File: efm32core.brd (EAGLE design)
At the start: 52.1 x 53.3 mm, 7 parts

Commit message: marching on
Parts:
- added C1, C2: (no value), maple-r5:UD-4X5,8_NICHICON
- added C3: 0.1uF, SparkFun-Capacitors:0603-CAP
- added PMIC1: MCP1700T-DIGITAL, maple-r5:SOT23
- added PMIC2: MCP1700T-ANALOG, maple-r5:SOT23
- added R1: 100, SparkFun-Resistors:0603-RES
- added S1: SWITCH-MOMENTARY-2SMD, SparkFun-Electromechanical:TACTILE_SWITCH_SMD
- added USB: PIXHAWK2_MOLEX-47346-0001, PX4FMUv1.7.1:PIXHAWK2_MOLEX-47346-0001
- moved U$7 12.0 mm to (33.5, 19.1), turned to 270 degrees
- moved U$5 8.90 mm to (5.54, 25.8)
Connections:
- new net 3.3V: C1.+, PMIC1.2
- new net GND: C1.-, C2.-, C3.1, PMIC1.1, PMIC2.1, R1.1, USB.GND, USB.GND1, USB.GND2, USB.GND3
- new net N$5: C3.2, S1.3, U$7.20
- new net N$6: R1.2, S1.1
- new net VDD: C2.+, PMIC2.2
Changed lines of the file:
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@@
 <layer number="54" name="bGND_GNDA" color="1" fill="9" visible="no" active="no"/>
 <layer number="56" name="wert" color="7" fill="1" visible="no" active="no"/>
+<layer number="57" name="tCAD" color="7" fill="1" visible="yes" active="yes"/>
+<layer number="58" name="bCAD" color="7" fill="1" visible="yes" active="yes"/>
 <layer number="91" name="Nets" color="2" fill="1" visible="no" active="no"/>
 <layer number="92" name="Busses" color="1" fill="1" visible="no" active="no"/>
@@
 <layer number="108" name="tplace-old" color="10" fill="1" visible="yes" active="yes"/>
 <layer number="109" name="ref-old" color="11" fill="1" visible="yes" active="yes"/>
+<layer number="110" name="fp0" color="7" fill="1" visible="yes" active="yes"/>
 <layer number="116" name="Patch_BOT" color="9" fill="4" visible="no" active="yes"/>
 <layer number="121" name="_tsilk" color="7" fill="1" visible="no" active="yes"/>
 <layer number="122" name="_bsilk" color="7" fill="1" visible="no" active="yes"/>
+<layer number="123" name="tTestmark" color="7" fill="1" visible="yes" active="yes"/>
+<layer number="124" name="bTestmark" color="7" fill="1" visible="yes" active="yes"/>
 <layer number="125" name="_tNames" color="7" fill="1" visible="yes" active="yes"/>
+<layer number="131" name="tAdjust" color="7" fill="1" visible="yes" active="yes"/>
+<layer number="132" name="bAdjust" color="7" fill="1" visible="yes" active="yes"/>
 <layer number="144" name="Drill_legend" color="7" fill="1" visible="yes" active="yes"/>
 <layer number="151" name="HeatSink" color="7" fill="1" visible="no" active="yes"/>
@@
 <wire x1="29.21" y1="50.8" x2="25.146" y2="50.8" width="0.254" layer="37"/>
 <wire x1="34.29" y1="2.54" x2="30.226" y2="2.54" width="0.254" layer="37"/>
-<wire x1="7.366" y1="50.8" x2="2.54" y2="50.8" width="0.254" layer="37"/>
 <dimension x1="49.53" y1="40.64" x2="49.53" y2="53.34" x3="61.468" y3="46.99" textsize="1.27" layer="37"/>
 <dimension x1="49.53" y1="2.54" x2="49.53" y2="0" x3="60.96" y3="1.27" textsize="1.27" layer="37"/>
@@
 </autorouter>
 <elements>
-<element name="U$5" library="gecko" package="GECKO_SOLDER_MASK_BOTTOM" value="" x="5.028" y="34.686" rot="MR0"/>
-<element name="U$7" library="EnergyMicro" package="QFP64" value="EFM32LG332F256" x="25.146" y="27.686"/>
+<element name="U$5" library="gecko" package="GECKO_SOLDER_MASK_BOTTOM" value="" x="5.536" y="25.796" rot="MR0"/>
+<element name="U$7" library="EnergyMicro" package="QFP64" value="EFM32LG332F256" x="33.528" y="19.05" rot="R270"/>
 <element name="JIOH" library="SparkFun-Connectors" package="1X08" value="" x="25.146" y="50.8" rot="R180"/>
 <element name="JIOL" library="SparkFun-Connectors" package="1X08" value="" x="46.99" y="50.8" rot="R180"/>
@@
 <element name="JPOWER" library="SparkFun-Connectors" package="1X06" value="" x="17.526" y="2.54"/>
 <element name="JEX" library="SparkFun-Connectors" package="2X8" value="M08X2" x="49.53" y="12.7" rot="R90"/>
+<element name="PMIC1" library="maple-r5" package="SOT23" value="MCP1700T-DIGITAL" x="10.922" y="9.398"/>
+<element name="PMIC2" library="maple-r5" package="SOT23" value="MCP1700T-ANALOG" x="15.24" y="9.398"/>
+<element name="C1" library="maple-r5" package="UD-4X5,8_NICHICON" value="" x="13.208" y="33.528" rot="R270"/>
+<element name="C2" library="maple-r5" package="UD-4X5,8_NICHICON" value="" x="13.208" y="41.148" rot="R90"/>
+<element name="S1" library="SparkFun-Electromechanical" package="TACTILE_SWITCH_SMD" value="SWITCH-MOMENTARY-2SMD" x="3.048" y="48.768" rot="R90"/>
+<element name="R1" library="SparkFun-Resistors" package="0603-RES" value="100" x="2.032" y="43.434" rot="R90">
+<attribute name="PROD_ID" value="RES-07863" x="2.032" y="43.434" size="1.778" layer="27" rot="R90" display="off"/>
+</element>
+<element name="C3" library="SparkFun-Capacitors" package="0603-CAP" value="0.1uF" x="4.572" y="43.434" rot="R90">
+<attribute name="PROD_ID" value="CAP-08604" x="4.572" y="43.434" size="1.778" layer="27" rot="R90" display="off"/>
+</element>
+<element name="USB" library="PX4FMUv1.7.1" package="PIXHAWK2_MOLEX-47346-0001" value="PIXHAWK2_MOLEX-47346-0001" x="2.286" y="7.112"/>
 </elements>
 <signals>
@@
 <contactref element="U$7" pad="22"/>
 <contactref element="U$7" pad="56"/>
-<wire x1="23.896" y1="21.936" x2="19.396" y2="27.936" width="0" layer="19" extent="16-16"/>
-<wire x1="25.396" y1="33.436" x2="19.396" y2="27.936" width="0" layer="19" extent="16-16"/>
+<wire x1="33.778" y1="24.8" x2="39.278" y2="18.8" width="0" layer="19" extent="1-1"/>
+<wire x1="27.778" y1="20.3" x2="33.778" y2="24.8" width="0" layer="19" extent="1-1"/>
 </signal>
 <signal name="N$1">
@@
 <contactref element="JPOWER" pad="1"/>
 </signal>
+<signal name="3.3V">
+<contactref element="PMIC1" pad="2"/>
+<contactref element="C1" pad="+"/>
+<wire x1="11.872" y1="8.298" x2="13.208" y2="31.849" width="0" layer="19" extent="1-1"/>
+</signal>
+<signal name="VDD">
+<contactref element="PMIC2" pad="2"/>
+<contactref element="C2" pad="+"/>
+<wire x1="16.19" y1="8.298" x2="13.208" y2="42.827" width="0" layer="19" extent="1-1"/>
+</signal>
+<signal name="GND">
+<contactref element="C1" pad="-"/>
+<contactref element="PMIC1" pad="1"/>
+<contactref element="PMIC2" pad="1"/>
+<contactref element="C2" pad="-"/>
+<contactref element="R1" pad="1"/>
+<contactref element="C3" pad="1"/>
+<contactref element="USB" pad="GND"/>
+<contactref element="USB" pad="GND1"/>
+<contactref element="USB" pad="GND2"/>
+<contactref element="USB" pad="GND3"/>
+<wire x1="13.208" y1="35.207" x2="13.208" y2="39.469" width="0" layer="19" extent="1-1"/>
+<wire x1="4.572" y1="42.584" x2="13.208" y2="39.469" width="0" layer="19" extent="1-1"/>
+<wire x1="2.032" y1="42.584" x2="4.572" y2="42.584" width="0" layer="19" extent="1-1"/>
+<wire x1="14.29" y1="8.298" x2="13.208" y2="35.207" width="0" layer="19" extent="1-1"/>
+<wire x1="9.972" y1="8.298" x2="14.29" y2="8.298" width="0" layer="19" extent="1-1"/>
+<wire x1="5.086" y1="5.812" x2="9.972" y2="8.298" width="0" layer="19" extent="1-1"/>
+<wire x1="4.586" y1="4.612" x2="5.086" y2="5.812" width="0" layer="19" extent="1-1"/>
+<wire x1="4.586" y1="9.612" x2="5.086" y2="5.812" width="0" layer="19" extent="1-1"/>
+<wire x1="2.286" y1="10.062" x2="4.586" y2="9.612" width="0" layer="19" extent="1-1"/>
+</signal>
+<signal name="N$5">
+<contactref element="U$7" pad="20"/>
+<contactref element="S1" pad="3"/>
+<contactref element="C3" pad="2"/>
+<wire x1="4.572" y1="44.284" x2="4.953" y2="46.228" width="0" layer="19" extent="1-1"/>
+<wire x1="27.778" y1="21.3" x2="4.572" y2="44.284" width="0" layer="19" extent="1-1"/>
+</signal>
+<signal name="N$6">
+<contactref element="S1" pad="1"/>
+<contactref element="R1" pad="2"/>
+<wire x1="2.032" y1="44.284" x2="1.143" y2="46.228" width="0" layer="19" extent="1-1"/>
+</signal>
 </signals>

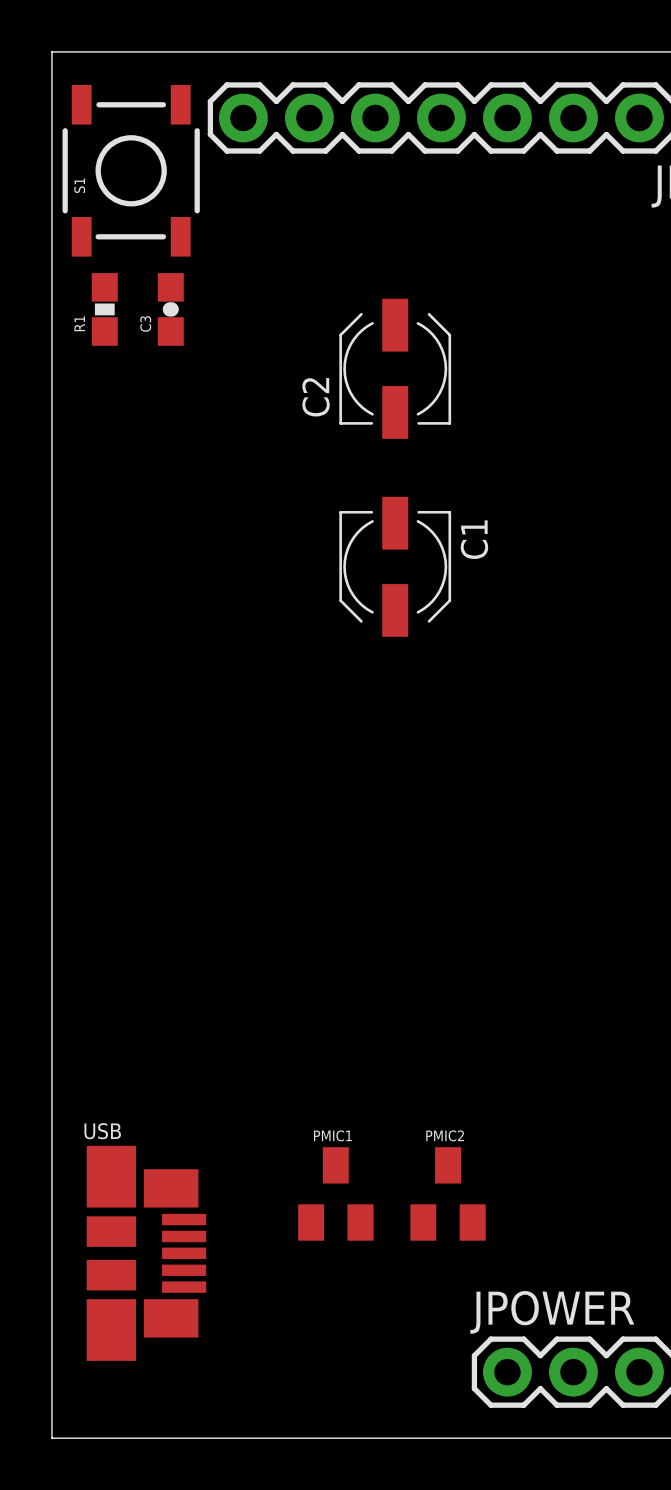
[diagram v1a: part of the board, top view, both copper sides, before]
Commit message: optimize board shape
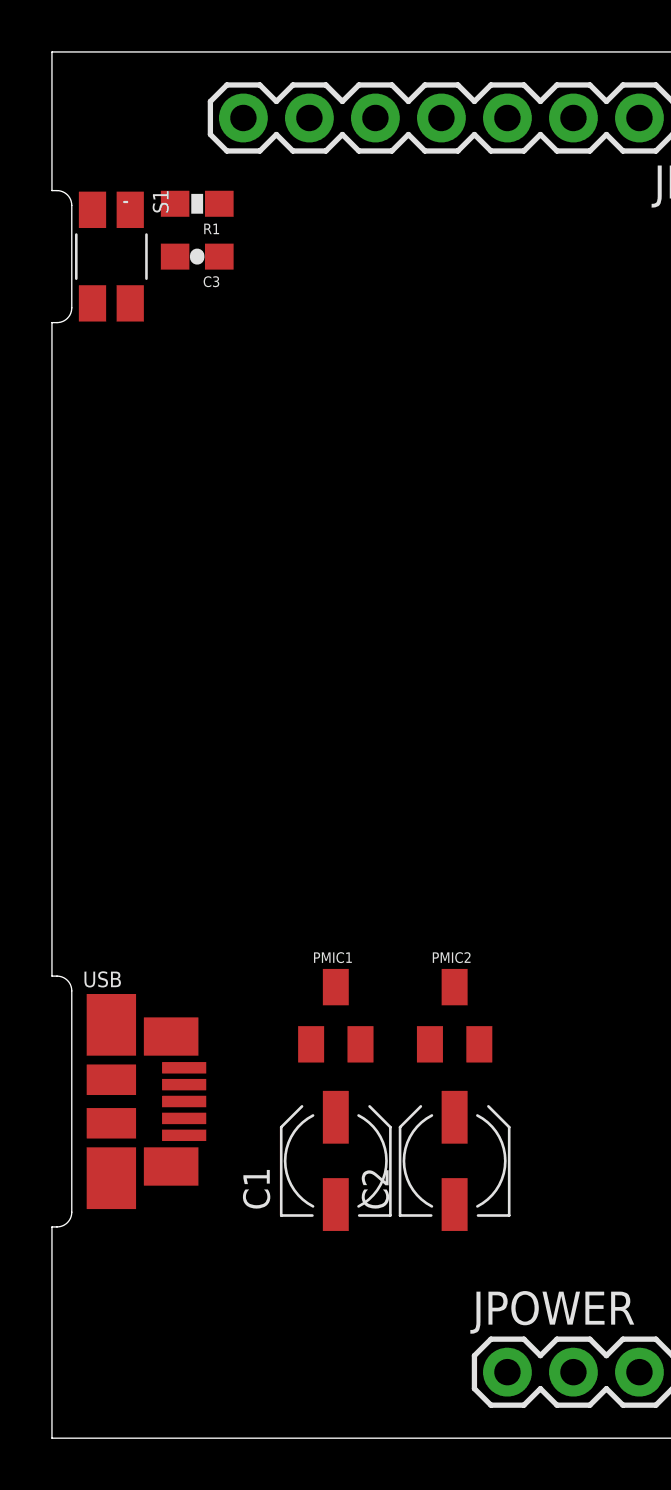
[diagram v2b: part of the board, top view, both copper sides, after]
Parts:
- S1: value SWITCH-MOMENTARY-2SMD -> PIXHAWK2_SWITCH-MOMENTARY-2; device SparkFun-Electromechanical:TACTILE_SWITCH_SMD -> PX4FMUv1.7.1:PIXHAWK2_EVQP7J01K
- moved C2 30.6 mm to (15.5, 10.7)
- moved U$5 29.6 mm to (34.4, 19.3), turned to 270 degrees
- moved C1 23.0 mm to (10.9, 10.7), turned to 90 degrees
- moved PMIC2 6.86 mm to (15.5, 16.3)
- moved PMIC1 6.86 mm to (10.9, 16.3)
- moved USB 5.84 mm to (2.29, 13.0)
- moved R1 5.40 mm to (5.59, 47.5), turned to 180 degrees
- moved S1 3.39 mm to (2.29, 45.5), turned to 270 degrees
- moved C3 2.27 mm to (5.59, 45.5), turned to 180 degrees
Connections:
- new net 5V: PMIC1.3, PMIC2.3, USB.VBUS
- net N$5: now also S1.B3; no longer S1.3
- net N$6: now also S1.A1; no longer S1.1
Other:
- outline, holes or cut-outs redrawn

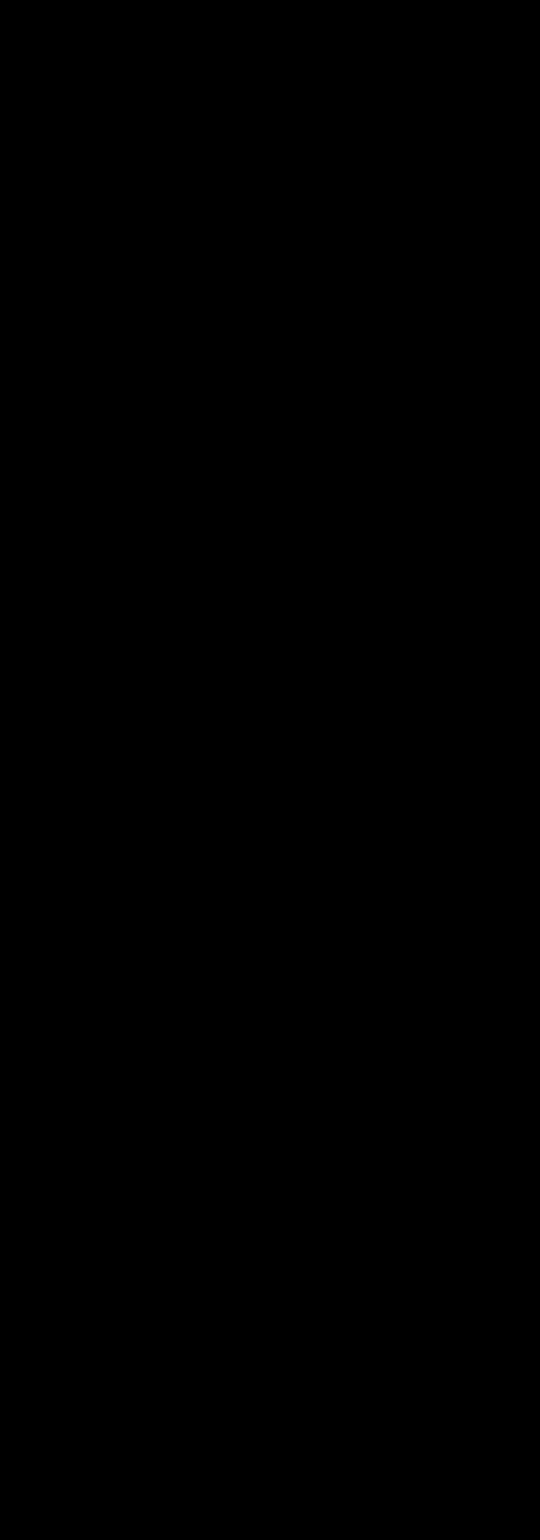
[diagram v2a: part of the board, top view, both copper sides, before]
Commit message: modulize, update power and usb
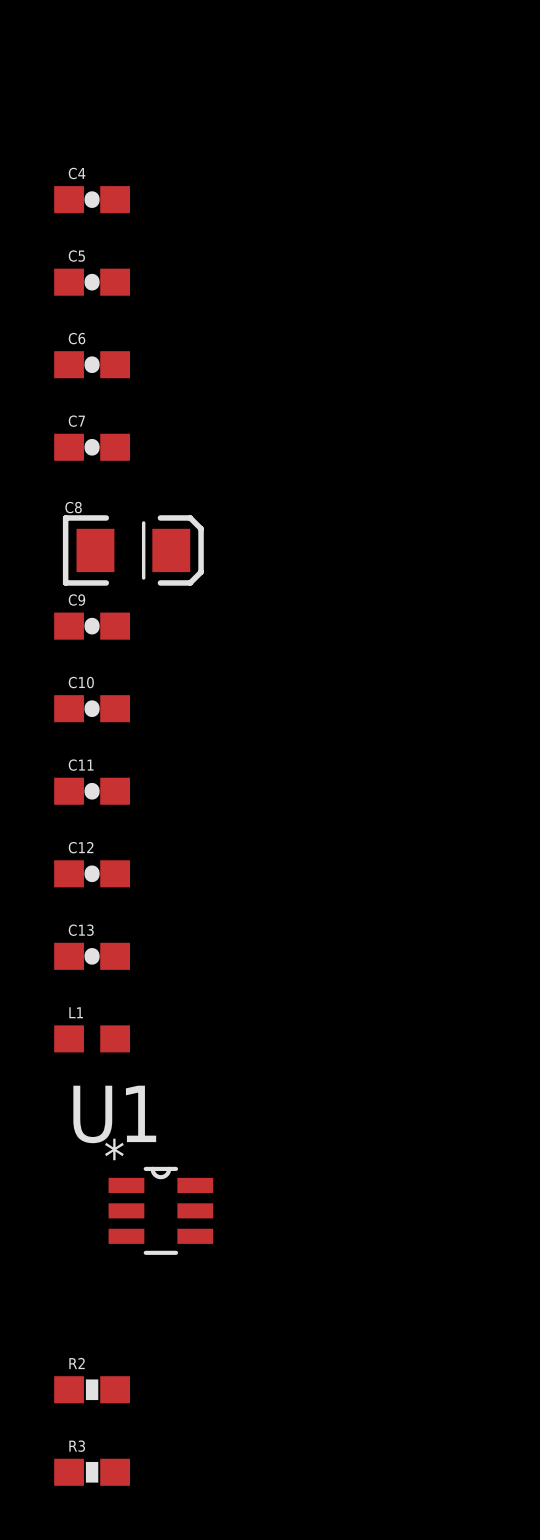
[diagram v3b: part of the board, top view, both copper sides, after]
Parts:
- added C10: 4.7uF, SparkFun-Capacitors:0603-CAP
- added C11, C12: 10nF, SparkFun-Capacitors:0603-CAP
- added C13: 10uF, SparkFun-Capacitors:0603-CAP
- added C4, C9: 1.0uF, SparkFun-Capacitors:0603-CAP
- added C5, C6, C7: 0.1uF, SparkFun-Capacitors:0603-CAP
- added C8: 10uF, SparkFun-Capacitors:EIA3216
- added L1: (no value), SparkFun-Passives:0603
- added R2, R3: 15R, SparkFun-Resistors:0603-RES
- added U1: IP4220CZ6SSOT-6, FT232H-basic:SOT95P275X110-6N
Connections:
- removed net AVDD_0: U$7.27
- removed net AVDD_1: U$7.23
- removed net DECOUPLE: U$7.40
- removed net IOVDD_0: U$7.7
- removed net IOVDD_3: U$7.26
- removed net IOVDD_5: U$7.55
- removed net USB_VBUS: U$7.52
- removed net USB_VREGI: U$7.45
- removed net USB_VREGO: U$7.46
- removed net VDD_DREG: U$7.39
- removed net VSS: U$7.22, U$7.56, U$7.8
- new net 1: L1.2, U1.5, USB.VBUS
- new net N$10: C11.1, C12.1, C13.1, U$7.23, U$7.27
- new net N$13: R3.2, U1.4, USB.D+
- new net N$14: R2.2, U1.6, USB.D-
- new net N$7: C4.1, U$7.40
- new net N$8: C9.2, U$7.46
- new net USB_DM: R2.1, U$7.47
- new net USB_DP: R3.1, U$7.48
- new net USB_ID: U$7.53, U1.1, USB.ID
- net 5V: now also C10.2, C5.2, C6.2, C7.2, C8.A, L1.1, U$7.26, U$7.39, U$7.45, U$7.52, U$7.55, U$7.7; no longer USB.VBUS
- net GND: now also C10.1, C11.2, C12.2, C13.2, C4.2, C5.1, C6.1, C7.1, C8.C, C9.1, U$7.22, U$7.56, U$7.8, U1.2, USB.GND4

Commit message: optimize a bit
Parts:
- added C14: 1uF, SparkFun-Capacitors:1206
- added STANDOFF1, STANDOFF2, STANDOFF3, STANDOFF4: STAND-OFF, SparkFun-Electromechanical:STAND-OFF
- C1, C2: value (none) -> 1uF; device maple-r5:UD-4X5,8_NICHICON -> SparkFun-Capacitors:1206
- C13: device SparkFun-Capacitors:0603-CAP -> SparkFun-Capacitors:1206
- C8: device SparkFun-Capacitors:EIA3216 -> SparkFun-Capacitors:1206
- moved C2 87.8 mm to (-13.7, -72.1), turned to 0 degrees
- moved C1 82.7 mm to (-13.7, -68.3), turned to 0 degrees
- moved C8 38.4 mm to (-13.7, -60.7)
- moved C13 27.1 mm to (-13.7, -64.5)
- moved USB 1.78 mm to (2.29, 11.2)
- moved C3 0.25 mm to (5.59, 45.2)
- moved R1 0.25 mm to (5.59, 47.2)
- moved S1 0.25 mm to (2.29, 45.2)
- renumbered U$5 to GECKO, U$7 to MCU
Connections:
- removed net N$4: JPOWER.1
- removed net N$5: C3.2, MCU.20, S1.B3
- new net ADCH0: MCU.28
- new net ADCH1: MCU.29
- new net ADCH2: MCU.30
- new net ADCH3: MCU.31
- new net ADCH4: MCU.32
- new net ADCH5: MCU.33
- new net PD6: MCU.34
- new net PD7: MCU.35
- new net PD8: MCU.36
- new net RESET: C3.2, JPOWER.1, MCU.20, S1.B3
- new net VIN: JPOWER.6
- net 3.3V: now also C1.1, JPOWER.2; no longer C1.+
- net 5V: now also C14.1, C8.2; no longer C8.A
- net GND: now also C1.2, C14.2, C2.2, C8.1, JPOWER.4, JPOWER.5; no longer C1.-, C2.-, C8.C
- net VDD: now also C2.1, JPOWER.3; no longer C2.+
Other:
- outline, holes or cut-outs redrawn

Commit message: update a bit
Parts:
- added R4, R5: 100, SparkFun-Resistors:0603-RES
- added S2: PIXHAWK2_SWITCH-MOMENTARY-2, PX4FMUv1.7.1:PIXHAWK2_EVQP7J01K
- moved STANDOFF4 148.8 mm to (49.5, 36.3)
- moved STANDOFF3 117.7 mm to (49.5, 6.86)
- moved S1 43.4 mm to (8.89, 2.29), turned to 0 degrees
- moved R1 41.7 mm to (6.86, 5.59), turned to 270 degrees
- moved C3 39.8 mm to (8.89, 5.59), turned to 270 degrees
- moved MCU 0.25 mm to (33.5, 19.3), turned to 0 degrees
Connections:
- new net N$5: R4.1
- net 3.3V: now also R5.2
- net ADCH0: now also JAD.1
- net ADCH1: now also JAD.2
- net ADCH2: now also JAD.3
- net ADCH3: now also JAD.4
- net ADCH4: now also JAD.5
- net ADCH5: now also JAD.6
- net N$2: now also R4.2, S2.A1; no longer JAD.1
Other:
- outline, holes or cut-outs redrawn

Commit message: layout components
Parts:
- added C15, C16: 7p5, SparkFun-Capacitors:0603-CAP
- added C17, C18: 18p, SparkFun-Capacitors:0603-CAP
- added L2: (no value), SparkFun-Passives:0603
- added R6: 100, SparkFun-Resistors:0603-RES
- added X1: 48.0MHz, adafruit:NX5032
- added X2: 32.768kHz, adafruit:NX5032
- moved C8 96.4 mm to (41.9, 18.0), turned to 270 degrees
- moved C14 94.4 mm to (12.7, 14.7)
- moved C2 90.1 mm to (24.1, 9.65), turned to 270 degrees
- moved C13 84.5 mm to (26.7, 9.65), turned to 270 degrees
- moved C1 84.2 mm to (18.0, 9.65), turned to 270 degrees
- moved C10 72.2 mm to (41.9, 23.6), turned to 180 degrees
- moved C9 71.5 mm to (41.9, 25.7), turned to 180 degrees
- moved R3 65.1 mm to (12.4, 4.83), turned to 180 degrees
- moved R2 64.2 mm to (12.4, 6.86), turned to 180 degrees
- moved C12 64.0 mm to (21.1, 22.1)
- moved C5 60.0 mm to (33.8, 30.2), turned to 270 degrees
- moved U1 59.0 mm to (10.4, 9.40)
- moved C4 58.8 mm to (41.9, 21.6)
- moved C11 58.5 mm to (31.0, 11.9), turned to 180 degrees
- moved L1 56.5 mm to (10.4, 12.4), turned to 180 degrees
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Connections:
- removed net N$10: C11.1, C12.1, C13.1, MCU.23, MCU.27
- new net HFXTAL_N: C15.1, MCU.25, X1.P$2
- new net HFXTAL_P: C16.1, MCU.24, X1.P$1
- new net LFXTAL_N: C18.1, MCU.16, X2.P$1
- new net LFXTAL_P: C17.1, MCU.15, X2.P$2
- new net N$4: L2.2, R6.1
- new net N$9: R5.1, S2.B3
- new net PA0: MCU.1
- net 3.3V: now also C5.2, C6.2, C7.2, C8.2, L2.1, MCU.26, MCU.39, MCU.55, MCU.7
- net 5V: no longer C5.2, C6.2, C7.2, C8.2, MCU.26, MCU.39, MCU.55, MCU.7
- net GND: now also C15.2, C16.2, C17.2, C18.2
- net VDD: now also C11.1, C12.1, C13.1, MCU.23, MCU.27, R6.2
